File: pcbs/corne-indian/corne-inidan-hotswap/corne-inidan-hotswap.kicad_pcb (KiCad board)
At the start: 2 copper layers, 277.2 x 107.5 mm, 56 parts, among them SW1 SW_Push

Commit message: Schematic is Done for Right side But Only switch & LED & placement
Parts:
- added D2: DSK34, Diode_SMD:D_SOD-123F, F.Cu at (210.0, 82.5)
- added MCU2: USB4105 - Type C USB 2.0 Connector, Connector_USB:USB_C_Receptacle_GCT_USB4105-xx-A_16P_TopMnt_Horizontal, B.Cu at (200.8, 110.2)
- added R4: 5K1, Resistor_SMD:R_0603_1608Metric, F.Cu at (199.5, 83.3)
- added R6: 5K1, Resistor_SMD:R_0603_1608Metric, F.Cu at (202.1, 83.3)
- added R7: 0R, Resistor_SMD:R_0603_1608Metric, F.Cu at (204.6, 83.3)
- added R8: 0R, Resistor_SMD:R_0603_1608Metric, F.Cu at (207.1, 83.3)
- added SW10: SW_Push, User_Button_Switch_Keyboard:SW_Cherry_MX_1.00u_Hotswap, F.Cu at (117.2, 147.9)
- added SW11: SW_Push, User_Button_Switch_Keyboard:SW_Cherry_MX_1.00u_Hotswap, F.Cu at (117.2, 128.8)
- added SW12: SW_Push, User_Button_Switch_Keyboard:SW_Cherry_MX_1.00u_Hotswap, F.Cu at (117.2, 109.5)
- added SW13: SW_Push, User_Button_Switch_Keyboard:SW_Cherry_MX_1.00u_Hotswap, F.Cu at (98.2, 111.8)
- added SW14: SW_Push, User_Button_Switch_Keyboard:SW_Cherry_MX_1.00u_Hotswap, F.Cu at (98.2, 131.0)
- added SW15: SW_Push, User_Button_Switch_Keyboard:SW_Cherry_MX_1.00u_Hotswap, F.Cu at (98.2, 150.2)
- added SW16: SW_Push, User_Button_Switch_Keyboard:SW_Cherry_MX_1.00u_Hotswap, F.Cu at (79.0, 155.0)
- added SW17: SW_Push, User_Button_Switch_Keyboard:SW_Cherry_MX_1.00u_Hotswap, F.Cu at (79.0, 135.8)
- added SW18: SW_Push, User_Button_Switch_Keyboard:SW_Cherry_MX_1.00u_Hotswap, F.Cu at (79.0, 116.5)
- added SW19: SW_Push, User_Button_Switch_Keyboard:SW_Cherry_MX_1.00u_Hotswap, F.Cu at (60.0, 116.5)
- added SW2: SW_Push, User_Button_Switch_Keyboard:SW_Cherry_MX_1.00u_Hotswap, F.Cu at (155.5, 152.2)
- added SW20: SW_Push, User_Button_Switch_Keyboard:SW_Cherry_MX_1.00u_Hotswap, F.Cu at (60.0, 135.8)
- added SW21: SW_Push, User_Button_Switch_Keyboard:SW_Cherry_MX_1.00u_Hotswap, F.Cu at (60.0, 155.0)
- added SW3: SW_Push, User_Button_Switch_Keyboard:SW_Cherry_MX_1.00u_Hotswap, F.Cu at (155.5, 133.6)
- added SW4: SW_Push, User_Button_Switch_Keyboard:SW_Cherry_MX_1.00u_Hotswap, F.Cu at (155.5, 114.2)
- added SW5: SW_Push, User_Button_Switch_Keyboard:SW_Cherry_MX_1.00u_Hotswap, F.Cu at (136.2, 112.0)
- added SW6: SW_Push, User_Button_Switch_Keyboard:SW_Cherry_MX_1.00u_Hotswap, F.Cu at (136.2, 131.2)
- added SW7: SW_Push, User_Button_Switch_Keyboard:SW_Cherry_MX_1.00u_Hotswap, F.Cu at (136.2, 150.5)
- added SW8: SW_Push, User_Button_Switch_Keyboard:SW_Cherry_MX_1.00u_Hotswap, F.Cu at (147.8, 173.7)
- added SW9: SW_Push, User_Button_Switch_Keyboard:SW_Cherry_MX_1.00u_Hotswap, F.Cu at (126.8, 171.5)
- added TP1: TestPoint, TestPoint:TestPoint_Pad_D1.0mm, F.Cu at (199.8, 79.7)
- added TP2: TestPoint, TestPoint:TestPoint_Pad_D1.0mm, F.Cu at (202.9, 79.7)
- added TP4: TestPoint, TestPoint:TestPoint_Pad_D1.0mm, F.Cu at (205.9, 79.7)
- added rSW1: SW_Push, User_Button_Switch_Keyboard:SW_Cherry_MX_1.50u_Hotswap, F.Cu at (207.8, 175.8)
- added rSW10: SW_Push, User_Button_Switch_Keyboard:SW_Cherry_MX_1.00u_Hotswap, F.Cu at (260.2, 147.8)
- added rSW11: SW_Push, User_Button_Switch_Keyboard:SW_Cherry_MX_1.00u_Hotswap, F.Cu at (260.2, 128.5)
- added rSW12: SW_Push, User_Button_Switch_Keyboard:SW_Cherry_MX_1.00u_Hotswap, F.Cu at (260.2, 109.2)
- added rSW13: SW_Push, User_Button_Switch_Keyboard:SW_Cherry_MX_1.00u_Hotswap, F.Cu at (279.5, 111.8)
- added rSW14: SW_Push, User_Button_Switch_Keyboard:SW_Cherry_MX_1.00u_Hotswap, F.Cu at (279.5, 131.0)
- added rSW15: SW_Push, User_Button_Switch_Keyboard:SW_Cherry_MX_1.00u_Hotswap, F.Cu at (279.5, 150.2)
- added rSW16: SW_Push, User_Button_Switch_Keyboard:SW_Cherry_MX_1.00u_Hotswap, F.Cu at (298.5, 155.0)
- added rSW17: SW_Push, User_Button_Switch_Keyboard:SW_Cherry_MX_1.00u_Hotswap, F.Cu at (298.5, 135.8)
- added rSW18: SW_Push, User_Button_Switch_Keyboard:SW_Cherry_MX_1.00u_Hotswap, F.Cu at (298.5, 116.5)
- added rSW19: SW_Push, User_Button_Switch_Keyboard:SW_Cherry_MX_1.00u_Hotswap, F.Cu at (317.6, 116.5)
- added rSW2: SW_Push, User_Button_Switch_Keyboard:SW_Cherry_MX_1.00u_Hotswap, F.Cu at (222.0, 152.2)
- added rSW20: SW_Push, User_Button_Switch_Keyboard:SW_Cherry_MX_1.00u_Hotswap, F.Cu at (317.8, 135.8)
- added rSW21: SW_Push, User_Button_Switch_Keyboard:SW_Cherry_MX_1.00u_Hotswap, F.Cu at (317.8, 155.0)
- added rSW3: SW_Push, User_Button_Switch_Keyboard:SW_Cherry_MX_1.00u_Hotswap, F.Cu at (222.0, 133.2)
- added rSW4: SW_Push, User_Button_Switch_Keyboard:SW_Cherry_MX_1.00u_Hotswap, F.Cu at (222.0, 114.0)
- added rSW5: SW_Push, User_Button_Switch_Keyboard:SW_Cherry_MX_1.00u_Hotswap, F.Cu at (241.0, 112.0)
- added rSW6: SW_Push, User_Button_Switch_Keyboard:SW_Cherry_MX_1.00u_Hotswap, F.Cu at (241.0, 131.2)
- added rSW7: SW_Push, User_Button_Switch_Keyboard:SW_Cherry_MX_1.00u_Hotswap, F.Cu at (241.0, 150.4)
- added rSW8: SW_Push, User_Button_Switch_Keyboard:SW_Cherry_MX_1.00u_Hotswap, F.Cu at (230.0, 173.5)
- added rSW9: SW_Push, User_Button_Switch_Keyboard:SW_Cherry_MX_1.00u_Hotswap, F.Cu at (251.0, 171.5)
- LED1, LED10, LED11, LED12, LED13, LED14, LED15, LED16, LED17, LED18, LED19, LED2, LED20, LED21, LED3, LED4, LED5, LED6, LED7, LED8, LED9, rLED1, rLED10, rLED11, rLED12, rLED13, rLED14, rLED15, rLED16, rLED17, rLED18, rLED19, rLED2, rLED20, rLED21, rLED3, rLED4, rLED5, rLED6, rLED7, rLED8, rLED9: value YS-SK6812MINI-E -> SK6812MINI-E; footprint kbd_local:YS-SK6812MINI-E -> User_Button_Switch_Keyboard:YS-SK6812MINI-E
- SW1: footprint Button_Switch_Keyboard:SW_Cherry_MX_1.50u_PCB -> User_Button_Switch_Keyboard:SW_Cherry_MX_1.50u_Hotswap
- moved D1 11.6 mm to (170.0, 85.0), turned to 0 degrees
- moved SW1 5.76 mm to (169.6, 175.9)
- moved R1 4.52 mm to (163.9, 80.2)
- moved R5 4.52 mm to (171.4, 80.2)
- moved R2 4.52 mm to (166.4, 80.2)
- moved R3 4.52 mm to (168.9, 80.2)
- moved TP10 4.52 mm to (185.3, 84.0)
- moved TP3 4.52 mm to (179.2, 84.0)
- moved TP9 4.52 mm to (182.3, 84.0)
- moved rLED8 0.96 mm to (231.5, 177.8)
- moved LED2 0.70 mm to (155.5, 156.5)
- moved LED1 0.62 mm to (173.8, 178.2)
- moved rLED20 0.60 mm to (317.8, 140.2)
- moved rLED13 0.58 mm to (279.5, 116.2)
- moved rLED12 0.58 mm to (260.2, 113.8)
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- renumbered GSM1 to MCU1
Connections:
- net /left/LED renamed /left/L_KEY
- net /right/LED renamed /Right/L_KEY
- net Net-(JP1-A) renamed /left/L_KEY19
- net Net-(LED1-DOUT) renamed /left/L_KEY2
- net Net-(LED10-DIN) renamed /left/L_KEY10
- net Net-(LED10-DOUT) renamed /left/L_KEY11
- net Net-(LED11-DOUT) renamed /left/L_KEY12
- net Net-(LED12-DOUT) renamed /left/L_KEY13
- net Net-(LED13-DOUT) renamed /left/L_KEY14
- net Net-(LED14-DOUT) renamed /left/L_KEY15
- net Net-(LED15-DOUT) renamed /left/L_KEY16
- net Net-(LED16-DOUT) renamed /left/L_KEY17
- net Net-(LED17-DOUT) renamed /left/L_KEY18
- net Net-(LED19-DOUT) renamed /left/L_KEY20
- net Net-(LED2-DOUT) renamed /left/L_KEY3
- net Net-(LED20-DOUT) renamed /left/L_KEY21
- net Net-(LED3-DOUT) renamed /left/L_KEY4
- net Net-(LED4-DOUT) renamed /left/L_KEY5
- net Net-(LED5-DOUT) renamed /left/L_KEY6
- net Net-(LED6-DOUT) renamed /left/L_KEY7
- net Net-(LED7-DOUT) renamed /left/L_KEY8
- net Net-(LED8-DOUT) renamed /left/L_KEY9
- net Net-(rJP1-A) renamed /Right/L_KEY19
- net Net-(rLED1-DOUT) renamed /Right/L_KEY2
- net Net-(rLED10-DIN) renamed /Right/L_KEY10
- net Net-(rLED10-DOUT) renamed /Right/L_KEY11
- net Net-(rLED11-DOUT) renamed /Right/L_KEY12
- net Net-(rLED12-DOUT) renamed /Right/L_KEY13
- net Net-(rLED13-DOUT) renamed /Right/L_KEY14
- net Net-(rLED14-DOUT) renamed /Right/L_KEY15
- net Net-(rLED15-DOUT) renamed /Right/L_KEY16
- net Net-(rLED16-DOUT) renamed /Right/L_KEY17
- net Net-(rLED17-DOUT) renamed /Right/L_KEY18
- net Net-(rLED19-DOUT) renamed /Right/L_KEY20
- net Net-(rLED2-DOUT) renamed /Right/L_KEY3
- net Net-(rLED20-DOUT) renamed /Right/L_KEY21
- net Net-(rLED3-DOUT) renamed /Right/L_KEY4
- net Net-(rLED4-DOUT) renamed /Right/L_KEY5
- net Net-(rLED5-DOUT) renamed /Right/L_KEY6
- net Net-(rLED6-DOUT) renamed /Right/L_KEY7
- net Net-(rLED7-DOUT) renamed /Right/L_KEY8
- net Net-(rLED8-DOUT) renamed /Right/L_KEY9
- LED1 pad 1: Net-(D1-K) -> /left/5V_L
- LED10 pad 1: Net-(D1-K) -> /left/5V_L
- LED11 pad 1: Net-(D1-K) -> /left/5V_L
- LED12 pad 1: Net-(D1-K) -> /left/5V_L
- LED13 pad 1: Net-(D1-K) -> /left/5V_L
- LED14 pad 1: Net-(D1-K) -> /left/5V_L
- LED15 pad 1: Net-(D1-K) -> /left/5V_L
- LED16 pad 1: Net-(D1-K) -> /left/5V_L
- LED17 pad 1: Net-(D1-K) -> /left/5V_L
- LED18 pad 1: Net-(D1-K) -> /left/5V_L
- LED19 pad 1: Net-(D1-K) -> /left/5V_L
- LED2 pad 1: Net-(D1-K) -> /left/5V_L
- LED20 pad 1: Net-(D1-K) -> /left/5V_L
- LED21 pad 1: Net-(D1-K) -> /left/5V_L
- LED21 pad 2: Net-(EXLED1-DIN) -> /left/L_KEY22
- LED3 pad 1: Net-(D1-K) -> /left/5V_L
- LED4 pad 1: Net-(D1-K) -> /left/5V_L
- LED5 pad 1: Net-(D1-K) -> /left/5V_L
- LED6 pad 1: Net-(D1-K) -> /left/5V_L
- LED7 pad 1: Net-(D1-K) -> /left/5V_L
- LED8 pad 1: Net-(D1-K) -> /left/5V_L
- LED9 pad 1: Net-(D1-K) -> /left/5V_L
- SW1 pad 1: unconnected-(SW1-Pad1) -> /left/KEY_1
- SW1 pad 2: unconnected-(SW1-Pad2) -> GND
- rLED1 pad 1: Net-(rD1-K) -> /Right/5V_L
- rLED1 pad 3: GNDR -> GND
- rLED10 pad 1: Net-(rD1-K) -> /Right/5V_L
- rLED10 pad 3: GNDR -> GND
- rLED11 pad 1: Net-(rD1-K) -> /Right/5V_L
- rLED11 pad 3: GNDR -> GND
- rLED12 pad 1: Net-(rD1-K) -> /Right/5V_L
- rLED12 pad 3: GNDR -> GND
- rLED13 pad 1: Net-(rD1-K) -> /Right/5V_L
- rLED13 pad 3: GNDR -> GND
- rLED14 pad 1: Net-(rD1-K) -> /Right/5V_L
- rLED14 pad 3: GNDR -> GND
- rLED15 pad 1: Net-(rD1-K) -> /Right/5V_L
- rLED15 pad 3: GNDR -> GND
- rLED16 pad 1: Net-(rD1-K) -> /Right/5V_L
- rLED16 pad 3: GNDR -> GND
- rLED17 pad 1: Net-(rD1-K) -> /Right/5V_L
- rLED17 pad 3: GNDR -> GND
- rLED18 pad 1: Net-(rD1-K) -> /Right/5V_L
- rLED18 pad 3: GNDR -> GND
- rLED19 pad 1: Net-(rD1-K) -> /Right/5V_L
- rLED19 pad 3: GNDR -> GND
- rLED2 pad 1: Net-(rD1-K) -> /Right/5V_L
- rLED2 pad 3: GNDR -> GND
- rLED20 pad 1: Net-(rD1-K) -> /Right/5V_L
- rLED20 pad 3: GNDR -> GND
- rLED21 pad 1: Net-(rD1-K) -> /Right/5V_L
- rLED21 pad 2: Net-(rEXLED1-DIN) -> /Right/L_KEY22
- rLED21 pad 3: GNDR -> GND
- rLED3 pad 1: Net-(rD1-K) -> /Right/5V_L
- rLED3 pad 3: GNDR -> GND
- rLED4 pad 1: Net-(rD1-K) -> /Right/5V_L
- rLED4 pad 3: GNDR -> GND
- rLED5 pad 1: Net-(rD1-K) -> /Right/5V_L
- rLED5 pad 3: GNDR -> GND
- rLED6 pad 1: Net-(rD1-K) -> /Right/5V_L
- rLED6 pad 3: GNDR -> GND
- rLED7 pad 1: Net-(rD1-K) -> /Right/5V_L
- rLED7 pad 3: GNDR -> GND
- rLED8 pad 1: Net-(rD1-K) -> /Right/5V_L
- rLED8 pad 3: GNDR -> GND
- rLED9 pad 1: Net-(rD1-K) -> /Right/5V_L
- rLED9 pad 3: GNDR -> GND
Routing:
- net GND: vias 0 -> 24
- added copper zone on B.Cu, net GND
- added copper zone on F.Cu, net GND
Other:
- outline, holes or cut-outs redrawn

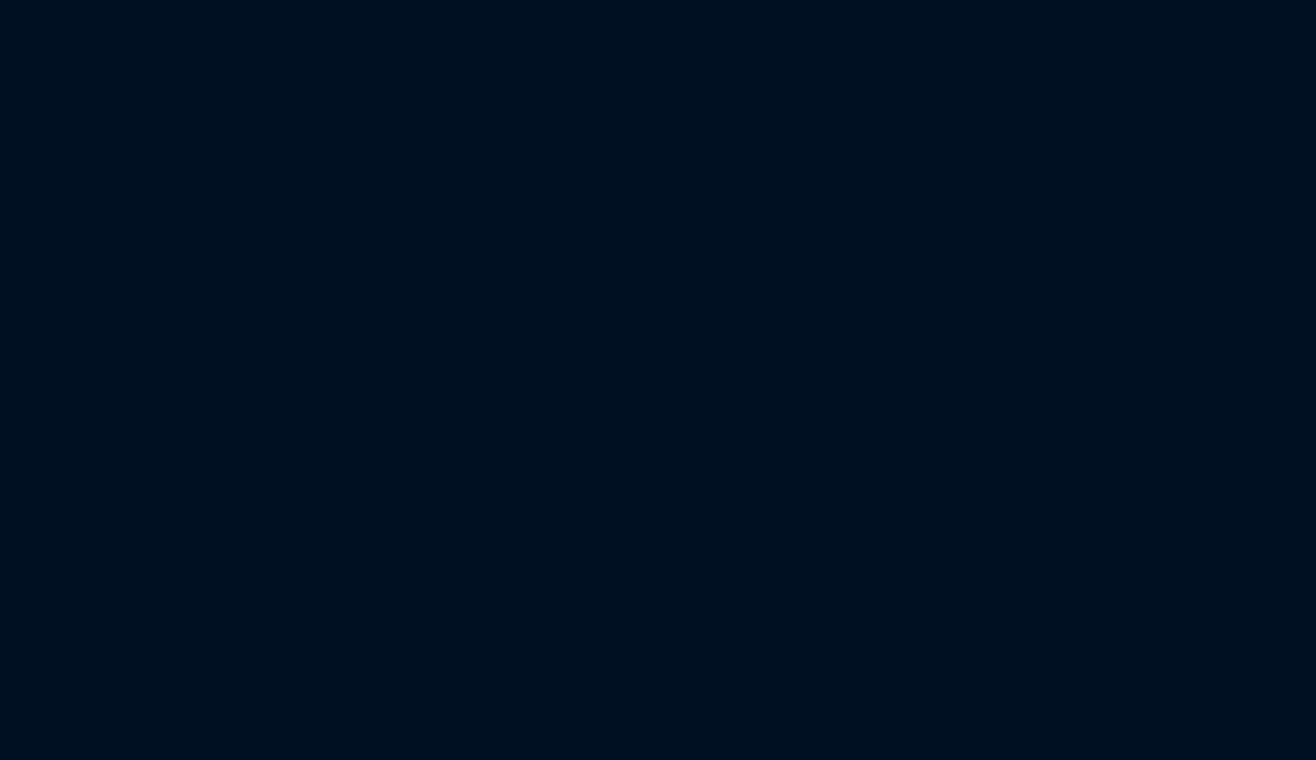
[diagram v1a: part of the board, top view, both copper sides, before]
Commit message: Rp2040 added to the shematic need to map to all Key Switch pins
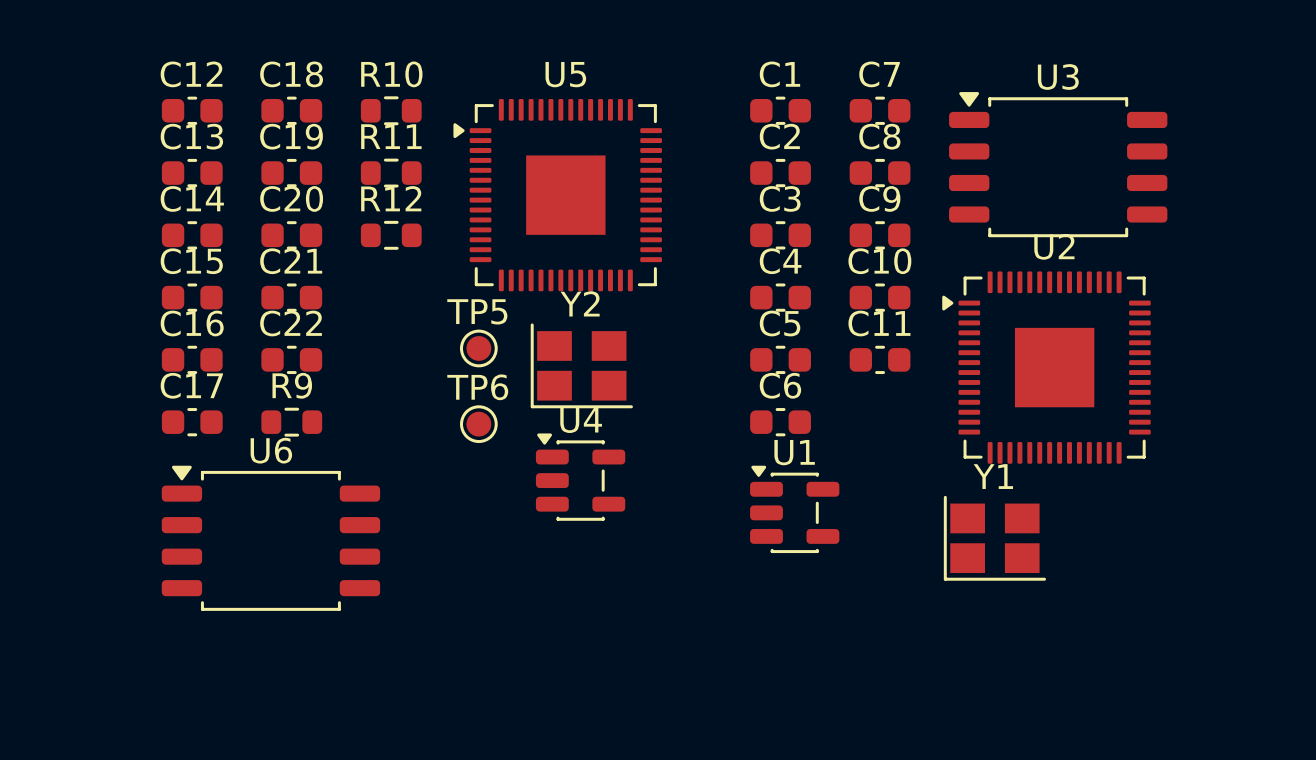
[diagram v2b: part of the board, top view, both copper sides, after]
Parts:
- added C1: 20pf, Capacitor_SMD:C_0603_1608Metric, F.Cu at (182.8, 48.8)
- added C10: 100nf, Capacitor_SMD:C_0603_1608Metric, F.Cu at (186.8, 56.3)
- added C11: 100nf, Capacitor_SMD:C_0603_1608Metric, F.Cu at (186.8, 58.8)
- added C12: 20pf, Capacitor_SMD:C_0603_1608Metric, F.Cu at (159.1, 48.8)
- added C13: 20pf, Capacitor_SMD:C_0603_1608Metric, F.Cu at (159.1, 51.3)
- added C14: 100nf, Capacitor_SMD:C_0603_1608Metric, F.Cu at (159.1, 53.8)
- added C15: 100nf, Capacitor_SMD:C_0603_1608Metric, F.Cu at (159.1, 56.3)
- added C16: 100nf, Capacitor_SMD:C_0603_1608Metric, F.Cu at (159.1, 58.8)
- added C17: 100nf, Capacitor_SMD:C_0603_1608Metric, F.Cu at (159.1, 61.4)
- added C18: 100nf, Capacitor_SMD:C_0603_1608Metric, F.Cu at (163.1, 48.8)
- added C19: 100nf, Capacitor_SMD:C_0603_1608Metric, F.Cu at (163.1, 51.3)
- added C2: 20pf, Capacitor_SMD:C_0603_1608Metric, F.Cu at (182.8, 51.3)
- added C20: 100nf, Capacitor_SMD:C_0603_1608Metric, F.Cu at (163.1, 53.8)
- added C21: 100nf, Capacitor_SMD:C_0603_1608Metric, F.Cu at (163.1, 56.3)
- added C22: 100nf, Capacitor_SMD:C_0603_1608Metric, F.Cu at (163.1, 58.8)
- added C3: 100nf, Capacitor_SMD:C_0603_1608Metric, F.Cu at (182.8, 53.8)
- added C4: 100nf, Capacitor_SMD:C_0603_1608Metric, F.Cu at (182.8, 56.3)
- added C5: 100nf, Capacitor_SMD:C_0603_1608Metric, F.Cu at (182.8, 58.8)
- added C6: 100nf, Capacitor_SMD:C_0603_1608Metric, F.Cu at (182.8, 61.4)
- added C7: 100nf, Capacitor_SMD:C_0603_1608Metric, F.Cu at (186.8, 48.8)
- added C8: 100nf, Capacitor_SMD:C_0603_1608Metric, F.Cu at (186.8, 51.3)
- added C9: 100nf, Capacitor_SMD:C_0603_1608Metric, F.Cu at (186.8, 53.8)
- added R10: 27R, Resistor_SMD:R_0603_1608Metric, F.Cu at (167.1, 48.8)
- added R11: 10K, Resistor_SMD:R_0603_1608Metric, F.Cu at (167.1, 51.3)
- added R12: 1K, Resistor_SMD:R_0603_1608Metric, F.Cu at (167.1, 53.8)
- added R9: 27R, Resistor_SMD:R_0603_1608Metric, F.Cu at (163.1, 61.4)
- added TP5: TestPoint, TestPoint:TestPoint_Pad_D1.0mm, F.Cu at (170.6, 58.4)
- added TP6: TestPoint, TestPoint:TestPoint_Pad_D1.0mm, F.Cu at (170.6, 61.4)
- added U1: AP2127K-3.3, Package_TO_SOT_SMD:SOT-23-5, F.Cu at (183.3, 65.0)
- added U2: RP2040, Package_DFN_QFN:QFN-56-1EP_7x7mm_P0.4mm_EP3.2x3.2mm, F.Cu at (193.8, 59.1)
- added U3: W25Q32JVSS, Package_SO:SOIC-8_5.3x5.3mm_P1.27mm, F.Cu at (194.0, 51.1)
- added U4: AP2127K-3.3, Package_TO_SOT_SMD:SOT-23-5, F.Cu at (174.7, 63.7)
- added U5: RP2040, Package_DFN_QFN:QFN-56-1EP_7x7mm_P0.4mm_EP3.2x3.2mm, F.Cu at (174.1, 52.2)
- added U6: W25Q32JVSS, Package_SO:SOIC-8_5.3x5.3mm_P1.27mm, F.Cu at (162.2, 66.1)
- added Y1: 12Mhz, Crystal:Crystal_SMD_Abracon_ABM8AIG-4Pin_3.2x2.5mm, F.Cu at (191.4, 66.0)
- added Y2: 12Mhz, Crystal:Crystal_SMD_Abracon_ABM8AIG-4Pin_3.2x2.5mm, F.Cu at (174.8, 59.1)
- R3: value 0R -> 27R
- R4: value 5K1 -> 27R
- R5: value 0R -> 10K
- R6: value 5K1 -> 1K
- R7, R8: value 0R -> 5K1
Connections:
- LED4 pad 2: /left/L_KEY5 -> /left/L_KEY6
- LED4 pad 4: /left/L_KEY4 -> /left/L_KEY5
- LED5 pad 2: /left/L_KEY6 -> /left/L_KEY5
- LED5 pad 4: /left/L_KEY5 -> /left/L_KEY4
- R4 pad 1: Net-(MCU2-CC1) -> /left/U_+
- R4 pad 2: GND -> /left/D+
- R5 pad 1: /left/U_+ -> +3.3V
- R5 pad 2: /left/D+ -> /left/SS
- R6 pad 1: Net-(MCU2-CC2) -> /left/SS
- R6 pad 2: GND -> /left/BOOT
- R7 pad 1: /Right/U_- -> Net-(MCU2-CC1)
- R7 pad 2: /Right/D- -> GND
- R8 pad 1: /Right/U_+ -> Net-(MCU2-CC2)
- R8 pad 2: /Right/D+ -> GND
- TP2 pad 1: /Right/D- -> /left/D-
- TP3 pad 1: +5V -> /left/D+
- TP4 pad 1: /Right/D+ -> +5V

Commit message: Mid of the renumbering & renaming
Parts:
- removed C1, C12, C13, C2: 20pf, Capacitor_SMD:C_0603_1608Metric
- removed C10, C11, C14, C15, C16, C17, C18, C19, C20, C21, C22, C3, C4, C5, C6, C7, C8, C9: 100nf, Capacitor_SMD:C_0603_1608Metric
- removed D1, D2: DSK34, Diode_SMD:D_SOD-123F
- removed R1, R2, R7, R8: 5K1, Resistor_SMD:R_0603_1608Metric
- removed R10, R3, R4, R9: 27R, Resistor_SMD:R_0603_1608Metric
- removed R11, R5: 10K, Resistor_SMD:R_0603_1608Metric
- removed R12, R6: 1K, Resistor_SMD:R_0603_1608Metric
- removed TP1, TP10, TP2, TP3, TP4, TP5, TP6, TP9: TestPoint, TestPoint:TestPoint_Pad_D1.0mm
- removed U1, U4: AP2127K-3.3, Package_TO_SOT_SMD:SOT-23-5
- removed U2, U5: RP2040, Package_DFN_QFN:QFN-56-1EP_7x7mm_P0.4mm_EP3.2x3.2mm
- removed U3, U6: W25Q32JVSS, Package_SO:SOIC-8_5.3x5.3mm_P1.27mm
- removed Y1, Y2: 12Mhz, Crystal:Crystal_SMD_Abracon_ABM8AIG-4Pin_3.2x2.5mm
- renumbered MCU2 to rMCU1

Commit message: Mid of the Placement still Rotary encoder is not done
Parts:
- added ?: , , F.Cu at (279.8, 101.2)
- added ?: , , F.Cu at (239.5, 101.2)
- added ?: , , F.Cu at (296.5, 166.0)
- added ?: , , F.Cu at (300.2, 166.0)
- added ?: , , F.Cu at (96.8, 101.2)
- added ?: , , F.Cu at (97.5, 101.2)
- added ?: , , F.Cu at (100.5, 101.2)
- added ?: , , F.Cu at (238.8, 101.2)
- added ?: , , F.Cu at (315.0, 166.0)
- added ?: , , F.Cu at (240.2, 101.2)
- added ?: , , F.Cu at (298.0, 166.0)
- added ?: , , F.Cu at (295.8, 166.0)
- added ?: , , F.Cu at (98.2, 101.2)
- added ?: , , F.Cu at (136.2, 101.2)
- added ?: , , F.Cu at (135.5, 101.2)
- added ?: , , F.Cu at (278.2, 101.2)
- added ?: , , F.Cu at (241.8, 101.2)
- added ?: , , F.Cu at (315.8, 166.0)
- added ?: , , F.Cu at (279.0, 101.2)
- added ?: , , F.Cu at (241.0, 101.2)
- added ?: , , F.Cu at (298.8, 166.0)
- added ?: , , F.Cu at (99.8, 101.2)
- added ?: , , F.Cu at (99.0, 101.2)
- added ?: , , F.Cu at (243.2, 101.2)
- added ?: , , F.Cu at (96.0, 101.2)
- added ?: , , F.Cu at (134.8, 101.2)
- added ?: , , F.Cu at (280.5, 101.2)
- added ?: , , F.Cu at (316.5, 166.0)
- added ?: , , F.Cu at (281.2, 101.2)
- added ?: , , F.Cu at (134.0, 101.2)
- added ?: , , F.Cu at (317.2, 166.0)
- added ?: , , F.Cu at (299.5, 166.0)
- added ?: , , F.Cu at (297.2, 166.0)
- added ?: , , F.Cu at (137.0, 101.2)
- added ?: , , F.Cu at (276.8, 101.2)
- added ?: , , F.Cu at (319.5, 166.0)
- added ?: , , F.Cu at (277.5, 101.2)
- added ?: , , F.Cu at (242.5, 101.2)
- added ?: , , F.Cu at (318.0, 166.0)
- added ?: , , F.Cu at (137.8, 101.2)
- added ?: , , F.Cu at (138.5, 101.2)
- added ?: , , F.Cu at (318.8, 166.0)
- added BOOT1: SKRKAGE020, Button:SW_Push_SPST_NO_Alps_SKRK, F.Cu at (156.5, 75.2)
- added C1: 20pf, Capacitor_SMD:C_0603_1608Metric, F.Cu at (112.8, 183.8)
- added C10: 100nf, Capacitor_SMD:C_0603_1608Metric, F.Cu at (127.3, 77.7)
- added C11: 100nf, Capacitor_SMD:C_0603_1608Metric, F.Cu at (127.3, 80.2)
- added C12: 100nf, Capacitor_SMD:C_0603_1608Metric, B.Cu at (169.5, 108.5)
- added C13: 100nf, Capacitor_SMD:C_0603_1608Metric, B.Cu at (161.5, 116.8)
- added C14: 100nf, Capacitor_SMD:C_0603_1608Metric, F.Cu at (169.5, 108.5)
- added C15: 100nf, Capacitor_SMD:C_0603_1608Metric, B.Cu at (163.0, 116.8)
- added C16: 10uf, Capacitor_SMD:C_0603_1608Metric, F.Cu at (169.5, 110.0)
- added C17: 10uf, Capacitor_SMD:C_0603_1608Metric, F.Cu at (170.2, 114.0)
- added C2: 20pf, Capacitor_SMD:C_0603_1608Metric, F.Cu at (112.8, 186.3)
- added C3: 100nf, Capacitor_SMD:C_0603_1608Metric, F.Cu at (110.5, 167.0)
- added C4: 100nf, Capacitor_SMD:C_0603_1608Metric, B.Cu at (108.8, 155.0)
- added C5: 100nf, Capacitor_SMD:C_0603_1608Metric, B.Cu at (113.2, 155.0)
- added C6: 100nf, Capacitor_SMD:C_0603_1608Metric, F.Cu at (111.0, 159.8)
- added C7: 100nf, Capacitor_SMD:C_0603_1608Metric, F.Cu at (111.0, 161.2)
- added C8: 100nf, Capacitor_SMD:C_0603_1608Metric, F.Cu at (127.3, 72.7)
- added C9: 100nf, Capacitor_SMD:C_0603_1608Metric, F.Cu at (127.3, 75.2)
- added D1: DSK34, Diode_SMD:D_SOD-123F, F.Cu at (174.2, 109.8)
- added J1: Conn_01x03_Pin, Connector_PinHeader_2.54mm:PinHeader_1x03_P2.54mm_Vertical, F.Cu at (148.7, 80.9)
- added J2: Conn_01x04_Pin, Connector_PinHeader_2.54mm:PinHeader_1x04_P2.54mm_Vertical, F.Cu at (179.3, 152.2)
- added J3: PJ-3136-B, Conn_Audio:PJ-3136-B, F.Cu at (178.5, 158.2)
- added J4: USB_A, Connector_USB:USB_A_Molex_67643_Horizontal, F.Cu at (71.5, 187.1)
- added J4: USB_A, Connector_USB:USB_A_Molex_67643_Horizontal, F.Cu at (93.1, 179.0)
- added J4: USB_A, Connector_USB:USB_A_Molex_67643_Horizontal, F.Cu at (92.5, 187.9)
- added J4: USB_A, Connector_USB:USB_A_Molex_67643_Horizontal, F.Cu at (62.1, 187.5)
- added MCU1: USB4105 - Type C USB 2.0 Connector, Connector_USB:USB_C_Receptacle_GCT_USB4105-xx-A_16P_TopMnt_Horizontal, F.Cu at (53.5, 173.5)
- added R1: 5K1, Resistor_SMD:R_0603_1608Metric, F.Cu at (176.5, 110.5)
- added R2: 5K1, Resistor_SMD:R_0603_1608Metric, F.Cu at (178.2, 110.5)
- added R3: 27R, Resistor_SMD:R_0603_1608Metric, B.Cu at (111.8, 155.0)
- added R4: 27R, Resistor_SMD:R_0603_1608Metric, B.Cu at (110.2, 155.0)
- added R5: 10K, Resistor_SMD:R_0603_1608Metric, F.Cu at (135.2, 72.8)
- added R6: 1K, Resistor_SMD:R_0603_1608Metric, F.Cu at (138.5, 72.8)
- added R7: 10K, Resistor_SMD:R_0603_1608Metric, F.Cu at (135.3, 77.7)
- added R8: 10K, Resistor_SMD:R_0603_1608Metric, F.Cu at (135.3, 80.2)
- added R9: 5K6, Resistor_SMD:R_0603_1608Metric, F.Cu at (135.3, 82.7)
- added RST1: SKRKAGE020, Button:SW_Push_SPST_NO_Alps_SKRK, F.Cu at (149.0, 75.2)
- added SW2: SW_Push, User_Button_Switch_Keyboard:SW_Cherry_MX_1.00u_Hotswap, F.Cu at (174.8, 143.2)
- added SW2: SW_Push, User_Button_Switch_Keyboard:SW_Cherry_MX_1.00u_Hotswap, F.Cu at (174.8, 124.0)
- added TP1: TestPoint, TestPoint:TestPoint_Pad_D1.0mm, F.Cu at (152.5, 80.2)
- added TP2: TestPoint, TestPoint:TestPoint_Pad_D1.0mm, F.Cu at (152.5, 83.2)
- added TP3: TestPoint, TestPoint:TestPoint_Pad_D1.0mm, F.Cu at (152.5, 86.2)
- added TP5: TestPoint, TestPoint:TestPoint_Pad_D1.0mm, F.Cu at (241.5, 80.5)
- added TP6: TestPoint, TestPoint:TestPoint_Pad_D1.0mm, F.Cu at (241.5, 83.5)
- added U1: AP2127K-3.3, Package_TO_SOT_SMD:SOT-23-5, F.Cu at (167.5, 113.5)
- added U2: RP2040, Package_DFN_QFN:QFN-56-1EP_7x7mm_P0.4mm_EP3.2x3.2mm, B.Cu at (113.5, 161.5)
- added U3: W25Q32JVSS, Package_SO:SOIC-8_5.3x5.3mm_P1.27mm, B.Cu at (124.8, 157.0)
- added U4: AMS1117-3.3, Package_TO_SOT_SMD:SOT-223-3_TabPin2, B.Cu at (167.5, 113.8)
- added U5: CH334F, Package_DFN_QFN:QFN-24-1EP_4x4mm_P0.5mm_EP2.7x2.7mm, F.Cu at (74.8, 174.8)
- added Y1: 12Mhz, Crystal:Crystal_SMD_Abracon_ABM8AIG-4Pin_3.2x2.5mm, B.Cu at (114.0, 169.0)
- added rBOOT1: SKRKAGE020, Button:SW_Push_SPST_NO_Alps_SKRK, F.Cu at (245.5, 71.5)
- added rC1: 20pf, Capacitor_SMD:C_0603_1608Metric, F.Cu at (265.8, 184.0)
- added rC10: 100nf, Capacitor_SMD:C_0603_1608Metric, F.Cu at (208.9, 78.4)
- added rC11: 100nf, Capacitor_SMD:C_0603_1608Metric, F.Cu at (208.9, 80.9)
- added rC12: 100nf, Capacitor_SMD:C_0603_1608Metric, B.Cu at (208.5, 107.8)
- added rC13: 100nf, Capacitor_SMD:C_0603_1608Metric, F.Cu at (211.0, 112.2)
- added rC14: 100nf, Capacitor_SMD:C_0603_1608Metric, B.Cu at (208.5, 109.2)
- added rC15: 100nf, Capacitor_SMD:C_0603_1608Metric, F.Cu at (225.8, 76.5)
- added rC16: 10uf, Capacitor_SMD:C_0603_1608Metric, F.Cu at (208.5, 107.8)
- added rC17: 10uf, Capacitor_SMD:C_0603_1608Metric, F.Cu at (224.5, 80.8)
- added rC2: 20pf, Capacitor_SMD:C_0603_1608Metric, F.Cu at (265.8, 186.5)
- added rC3: 100nf, Capacitor_SMD:C_0603_1608Metric, F.Cu at (261.0, 166.5)
- added rC4: 100nf, Capacitor_SMD:C_0603_1608Metric, B.Cu at (259.8, 156.2)
- added rC5: 100nf, Capacitor_SMD:C_0603_1608Metric, B.Cu at (263.5, 155.0)
- added rC6: 100nf, Capacitor_SMD:C_0603_1608Metric, F.Cu at (204.9, 85.9)
- added rC7: 100nf, Capacitor_SMD:C_0603_1608Metric, F.Cu at (204.9, 88.4)
- added rC8: 100nf, Capacitor_SMD:C_0603_1608Metric, F.Cu at (208.9, 73.3)
- added rC9: 100nf, Capacitor_SMD:C_0603_1608Metric, F.Cu at (208.9, 75.8)
- added rD1: DSK34, Diode_SMD:D_SOD-123F, F.Cu at (203.2, 109.8)
- added rJ1: Conn_01x03_Pin, Connector_PinHeader_2.54mm:PinHeader_1x03_P2.54mm_Vertical, F.Cu at (237.8, 77.4)
- added rJ2: Conn_01x04_Pin, Connector_PinHeader_2.54mm:PinHeader_1x04_P2.54mm_Vertical, F.Cu at (206.8, 152.0)
- added rJ3: PJ-3136-B, Conn_Audio:PJ-3136-B, F.Cu at (198.8, 158.5)
- added rR1: 5K1, Resistor_SMD:R_0603_1608Metric, F.Cu at (199.5, 110.8)
- added rR2: 5K1, Resistor_SMD:R_0603_1608Metric, F.Cu at (201.2, 110.8)
- added rR3: 27R, Resistor_SMD:R_0603_1608Metric, B.Cu at (252.8, 152.8)
- added rR4: 27R, Resistor_SMD:R_0603_1608Metric, B.Cu at (251.2, 152.8)
- added rR5: 10K, Resistor_SMD:R_0603_1608Metric, F.Cu at (216.9, 73.3)
- added rR6: 1K, Resistor_SMD:R_0603_1608Metric, F.Cu at (216.9, 75.8)
- added rR7: 10K, Resistor_SMD:R_0603_1608Metric, F.Cu at (216.9, 78.4)
- added rR8: 10K, Resistor_SMD:R_0603_1608Metric, F.Cu at (216.9, 80.9)
- added rR9: 5K6, Resistor_SMD:R_0603_1608Metric, F.Cu at (216.9, 83.4)
- added rRST1: SKRKAGE020, Button:SW_Push_SPST_NO_Alps_SKRK, F.Cu at (238.8, 71.5)
- added rSW2: SW_Push, User_Button_Switch_Keyboard:SW_Cherry_MX_1.00u_Hotswap, F.Cu at (202.8, 143.1)
- added rSW2: SW_Push, User_Button_Switch_Keyboard:SW_Cherry_MX_1.00u_Hotswap, F.Cu at (202.8, 123.9)
- added rTP1: TestPoint, TestPoint:TestPoint_Pad_D1.0mm, F.Cu at (241.5, 76.5)
- added rU1: AP2127K-3.3, Package_TO_SOT_SMD:SOT-23-5, F.Cu at (208.2, 111.9)
- added rU2: RP2040, Package_DFN_QFN:QFN-56-1EP_7x7mm_P0.4mm_EP3.2x3.2mm, B.Cu at (263.8, 161.5)
- added rU3: W25Q32JVSS, Package_SO:SOIC-8_5.3x5.3mm_P1.27mm, B.Cu at (269.0, 152.8)
- added rU4: AMS1117-3.3, Package_TO_SOT_SMD:SOT-223-3_TabPin2, B.Cu at (215.8, 122.5)
- added rY1: 12Mhz, Crystal:Crystal_SMD_Abracon_ABM8AIG-4Pin_3.2x2.5mm, F.Cu at (264.1, 169.4)
- moved EXLED2 0.45 mm to (174.8, 147.5)
- moved EXLED1 0.43 mm to (174.8, 128.5)
- moved rEXLED2 0.20 mm to (202.8, 147.5)
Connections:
- net +5V renamed VBUS
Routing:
- net +3.3V: track 0.00 -> 33.2 mm
- net /Right/SD0: track 0.00 -> 14.9 mm, vias 0 -> 2
- net /Right/D-: track 0.00 -> 14.5 mm
- net /Right/D+: track 0.00 -> 14.4 mm
- net /Right/SCLK: track 0.00 -> 14.1 mm, vias 0 -> 2
- net /Right/SD3: track 0.00 -> 11.7 mm, vias 0 -> 2
- net /Right/SD2: track 0.00 -> 10.9 mm, vias 0 -> 2
- net /Right/SS: track 0.00 -> 8.37 mm, vias 0 -> 2
- net /Right/SD1: track 0.00 -> 7.91 mm, vias 0 -> 2
- net /left/SD3: track 0.00 -> 6.33 mm, vias 0 -> 1
- net Net-(rU2-VREG_VOUT): track 0.00 -> 6.12 mm
- net /left/SCLK: track 0.00 -> 5.98 mm, vias 0 -> 1
- net /left/SD0: track 0.00 -> 5.52 mm
- net /left/SD2: track 0.00 -> 4.71 mm
- net /left/SD1: track 0.00 -> 3.90 mm
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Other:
- outline, holes or cut-outs redrawn
